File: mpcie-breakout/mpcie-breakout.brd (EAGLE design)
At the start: 50 x 70 mm, 37 parts, among them K1 694108106102, U1 IP4234CZ6, U2 LD1085D2T33R, X1 MPCIE-JAE, X2 MINI-USB-SHIELD-UX60-MB-5ST

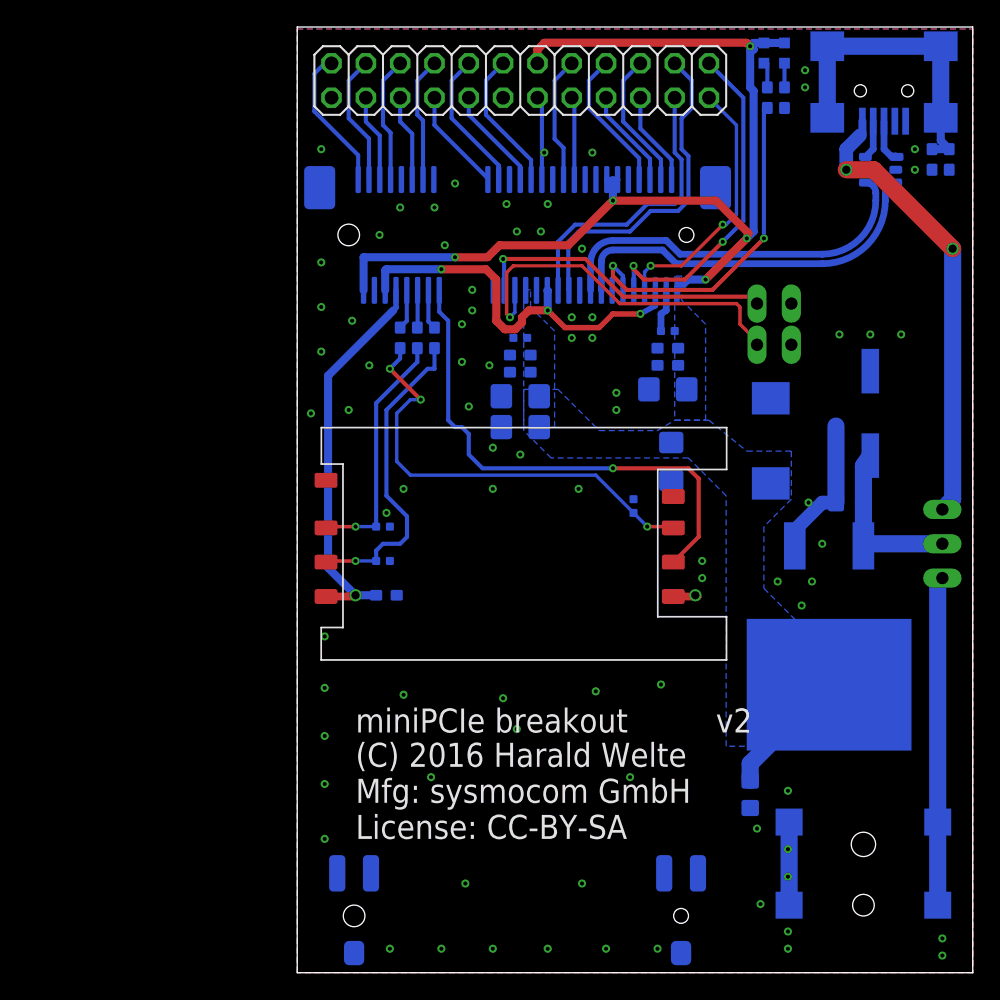
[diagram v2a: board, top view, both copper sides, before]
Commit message: mpcie-breakout: Enlarge to 70x70mm, add SMA, U.FL and Mounting Holes
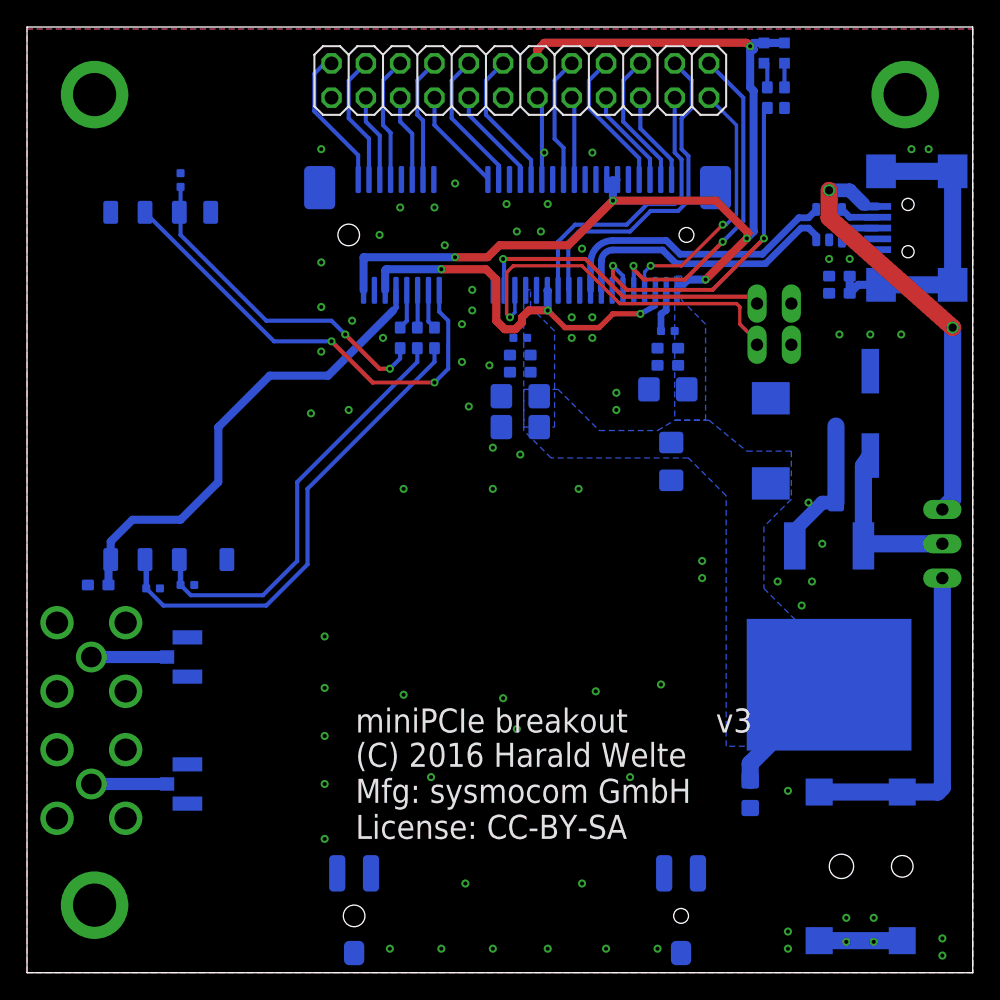
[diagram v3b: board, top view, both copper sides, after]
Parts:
- added X3, X4: (no value), laforge:SMA-F-S-TH
- added X5, X6: (no value), laforge:HRS_UFL
- moved C7 41.3 mm to (-8.64, 58.7)
- moved SIM1 27.5 mm to (-9.91, 43.4), flipped to the bottom, turned to 270 degrees
- moved C8 21.3 mm to (-14.7, 28.7), turned to 180 degrees
- moved C6 17.1 mm to (-10.7, 28.4)
- moved C5 15.1 mm to (-8.13, 28.7)
- moved C9 12.8 mm to (40.1, 50.3), turned to 180 degrees
- moved K1 11.1 mm to (49.8, 7.87), turned to 0 degrees
- moved R4 11.0 mm to (40.1, 51.6), turned to 180 degrees
- moved X2 10.3 mm to (45.2, 55.1), turned to 0 degrees
- moved U1 5.57 mm to (39.4, 55.4), turned to 0 degrees
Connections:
- new net N$13: X3.C, X5.SIG
- new net N$14: X4.C, X6.SIG
- net GND: now also X3.G1, X3.G2, X3.G3, X3.G4, X4.G1, X4.G2, X4.G3, X4.G4, X5.GND@1, X5.GND@2, X6.GND@1, X6.GND@2
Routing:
- net USIM_CLK: track 18.2 -> 31.4 mm, vias 1 -> 0
- net USIM_RESET: track 23.6 -> 35.8 mm, vias 1 -> 0
- net USIM_DATA: track 33.6 -> 25.1 mm, vias 3 -> 2
- net USB_D_P: track 27.5 -> 20.4 mm
- net USB_D_N: track 27.6 -> 21.2 mm
- net USIM_POWER: track 29.2 -> 35.2 mm, vias 1 -> 0
- net N$14: track 0.00 -> 5.61 mm
- net N$13: track 0.00 -> 5.61 mm
- net USIM_VPP: track 38.1 -> 34.2 mm, vias 1 -> 2
- net GND: track 28.3 -> 26.3 mm, vias 82 -> 83
- net USB_VBUS: track 35.4 -> 33.5 mm
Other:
- board size 50 x 70 mm -> 70 x 70 mm

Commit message: mpcie-breakout: Add third U.FL-SMA group
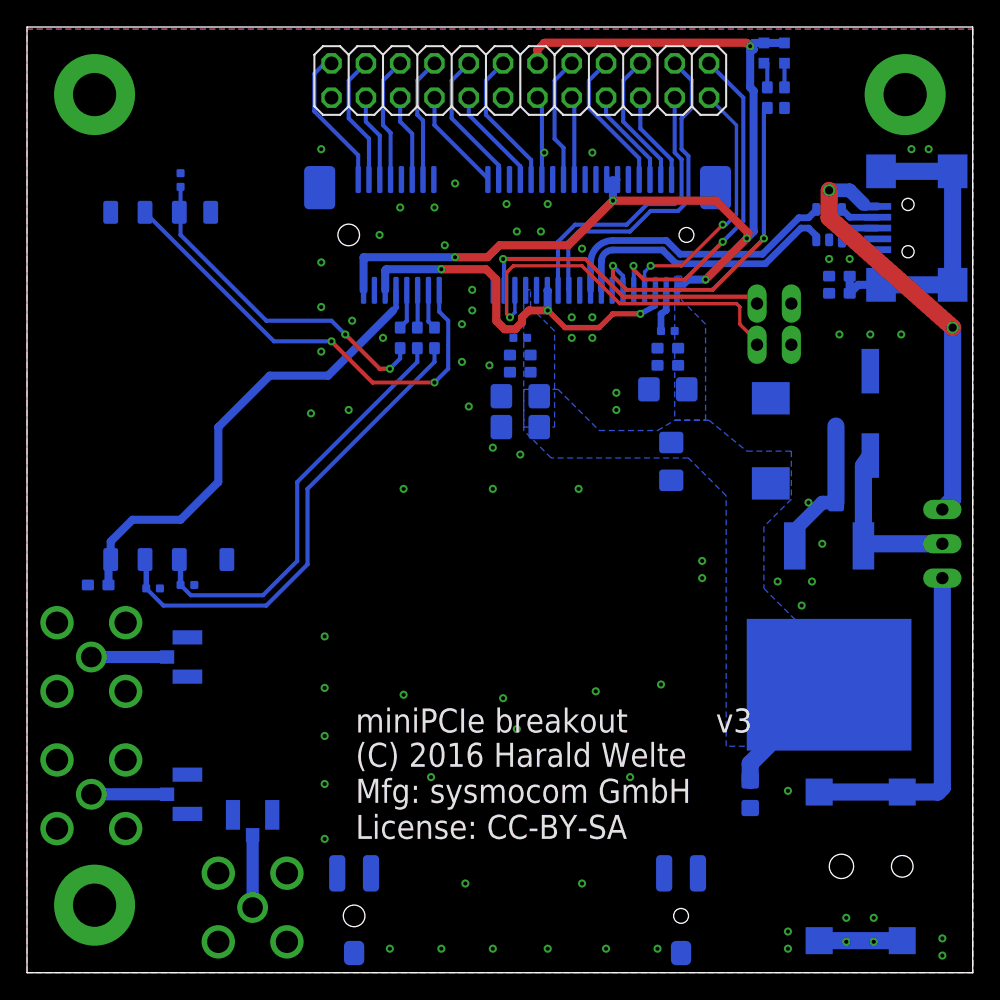
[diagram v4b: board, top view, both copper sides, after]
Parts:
- removed X6: (no value), laforge:HRS_UFL
- added Y3, Y4, Y5: (no value), laforge:HRS_UFL
- X5: device laforge:HRS_UFL -> laforge:SMA-F-S-TH
- moved X5 19.2 mm to (-3.30, 4.83), turned to 0 degrees
- moved X4 0.76 mm to (-15.2, 13.2)
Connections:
- new net N$7: X5.C, Y5.SIG
- net GND: now also X5.G1, X5.G2, X5.G3, X5.G4, Y3.GND@1, Y3.GND@2, Y4.GND@1, Y4.GND@2, Y5.GND@1, Y5.GND@2; no longer X5.GND@1, X5.GND@2, X6.GND@1, X6.GND@2
- net N$13: now also Y3.SIG; no longer X5.SIG
- net N$14: now also Y4.SIG; no longer X6.SIG
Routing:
- net N$7: track 0.00 -> 5.36 mm
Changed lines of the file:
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@@
 </element>
 <element name="X3" library="laforge" package="SMA-F-S-TH" value="" x="-15.24" y="23.368" rot="MR0"/>
-<element name="X4" library="laforge" package="SMA-F-S-TH" value="" x="-15.24" y="13.97" rot="MR180"/>
-<element name="X5" library="laforge" package="HRS_UFL" value="" x="-8.128" y="23.368" rot="MR90">
+<element name="X4" library="laforge" package="SMA-F-S-TH" value="" x="-15.24" y="13.208" rot="MR180"/>
+<element name="Y3" library="laforge" package="HRS_UFL" value="" x="-8.128" y="23.368" rot="MR90">
 <attribute name="OC_DIGIKEY" value="H9161CT-ND" x="-8.128" y="23.368" size="1.778" layer="28" rot="MR90" display="off"/>
 </element>
-<element name="X6" library="laforge" package="HRS_UFL" value="" x="-8.128" y="13.97" rot="MR90">
-<attribute name="OC_DIGIKEY" value="H9161CT-ND" x="-8.128" y="13.97" size="1.778" layer="28" rot="MR90" display="off"/>
+<element name="Y4" library="laforge" package="HRS_UFL" value="" x="-8.128" y="13.208" rot="MR90">
+<attribute name="OC_DIGIKEY" value="H9161CT-ND" x="-8.128" y="13.208" size="1.778" layer="28" rot="MR90" display="off"/>
+</element>
+<element name="X5" library="laforge" package="SMA-F-S-TH" value="" x="-3.302" y="4.826" rot="MR0"/>
+<element name="Y5" library="laforge" package="HRS_UFL" value="" x="-3.302" y="11.684" rot="MR0">
+<attribute name="OC_DIGIKEY" value="H9161CT-ND" x="-3.302" y="11.684" size="1.778" layer="28" rot="MR0" display="off"/>
 </element>
 </elements>
@@
 <contactref element="C11" pad="1"/>
 <contactref element="X3" pad="G1"/>
-<contactref element="X5" pad="GND@1"/>
+<contactref element="Y3" pad="GND@1"/>
 <contactref element="X3" pad="G2"/>
 <contactref element="X3" pad="G3"/>
 <contactref element="X3" pad="G4"/>
-<contactref element="X5" pad="GND@2"/>
+<contactref element="Y3" pad="GND@2"/>
 <contactref element="X4" pad="G1"/>
-<contactref element="X6" pad="GND@1"/>
+<contactref element="Y4" pad="GND@1"/>
 <contactref element="X4" pad="G2"/>
 <contactref element="X4" pad="G3"/>
 <contactref element="X4" pad="G4"/>
-<contactref element="X6" pad="GND@2"/>
-<via x="-15" y="5" extent="1-16" drill="3.2" diameter="5"/>
-<via x="-15" y="65" extent="1-16" drill="3.2" diameter="5"/>
-<via x="45" y="65" extent="1-16" drill="3.2" diameter="5"/>
+<contactref element="Y4" pad="GND@2"/>
+<via x="-15" y="5" extent="1-16" drill="3.2" diameter="6"/>
+<via x="-15" y="65" extent="1-16" drill="3.2" diameter="6"/>
+<via x="45" y="65" extent="1-16" drill="3.2" diameter="6"/>
+<contactref element="X5" pad="G1"/>
+<contactref element="Y5" pad="GND@1"/>
+<contactref element="X5" pad="G2"/>
+<contactref element="X5" pad="G3"/>
+<contactref element="X5" pad="G4"/>
+<contactref element="Y5" pad="GND@2"/>
 </signal>
 <signal name="USIM_POWER" class="3">
@@
 <signal name="N$13" class="2">
 <contactref element="X3" pad="C"/>
-<contactref element="X5" pad="SIG"/>
+<contactref element="Y3" pad="SIG"/>
 <wire x1="-15.24" y1="23.368" x2="-9.6305" y2="23.368" width="0.9" layer="16"/>
 </signal>
 <signal name="N$14" class="2">
 <contactref element="X4" pad="C"/>
-<contactref element="X6" pad="SIG"/>
-<wire x1="-15.24" y1="13.97" x2="-9.6305" y2="13.97" width="0.9" layer="16"/>
+<contactref element="Y4" pad="SIG"/>
+<wire x1="-15.24" y1="13.208" x2="-9.6305" y2="13.208" width="0.9" layer="16"/>
+</signal>
+<signal name="N$7" class="2">
+<contactref element="X5" pad="C"/>
+<contactref element="Y5" pad="SIG"/>
+<wire x1="-3.302" y1="10.1815" x2="-3.302" y2="4.826" width="0.9" layer="16"/>
 </signal>
 </signals>

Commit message: mcie-breakout: Align bLabels, more vias, cosmetics
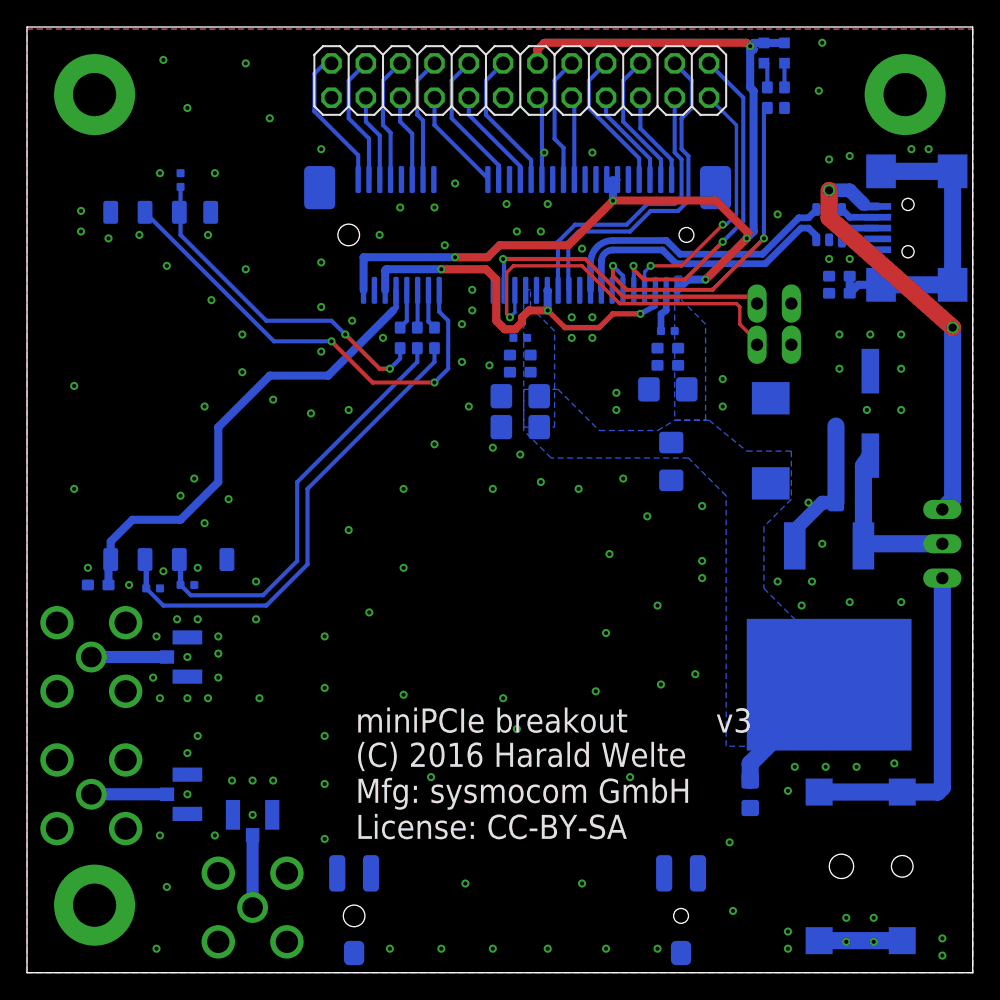
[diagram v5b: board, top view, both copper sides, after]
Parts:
- turned X3 to 180 degrees
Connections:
- net N$4 renamed PERST
- net N$6 renamed W_DISABLE
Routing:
- net GND: vias 83 -> 167
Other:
- board text added: "5V DC"
- board text added: "DC IN"
- board text added: "PERST"
- board text added: "USB"
- board text added: "W_DIS"

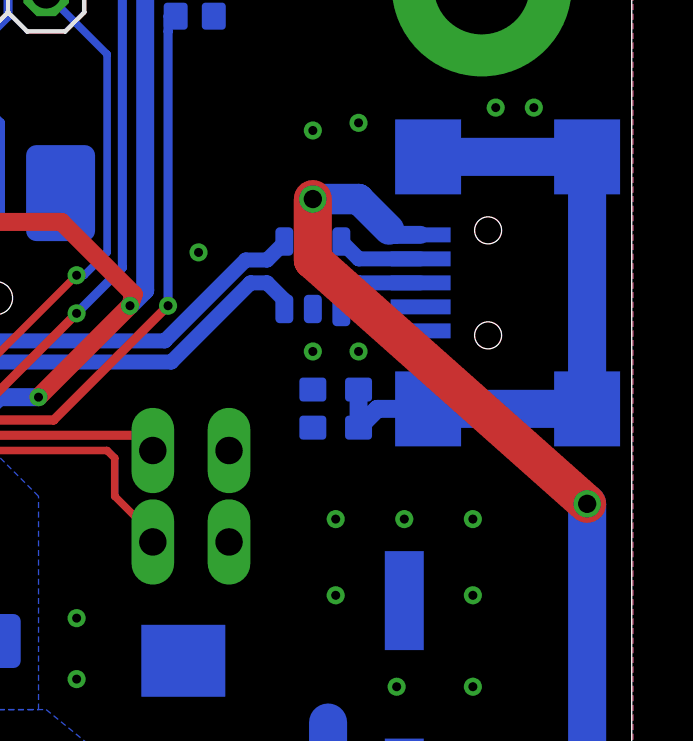
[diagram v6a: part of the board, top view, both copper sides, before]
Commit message: mpcie-breakout: USB_VBUS second parallel via to reduce impedance
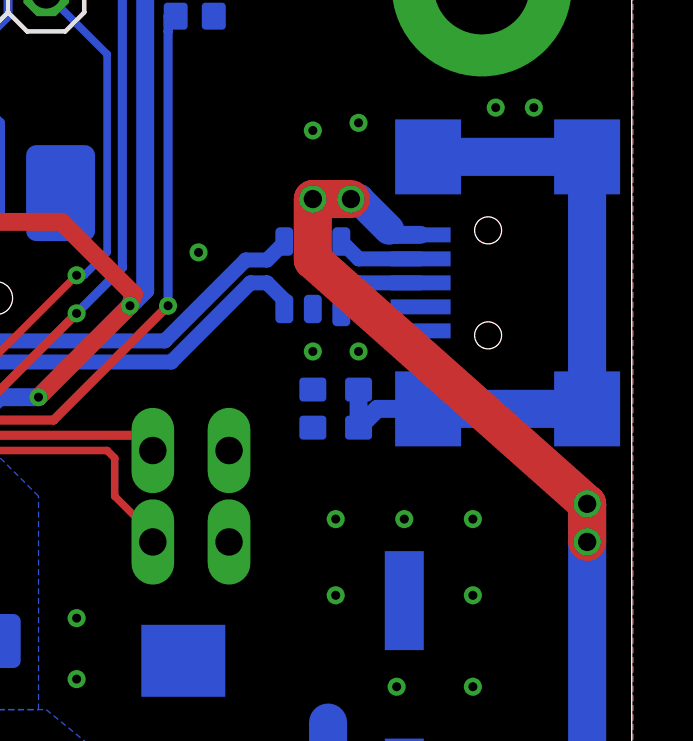
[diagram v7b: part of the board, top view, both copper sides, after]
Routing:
- net USB_VBUS: track 33.5 -> 36.1 mm, vias 2 -> 4
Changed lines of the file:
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@@
 <via x="39.37" y="57.912" extent="1-16" drill="0.6096"/>
 <wire x1="39.37" y1="57.912" x2="40.894" y2="57.912" width="1.016" layer="16"/>
+<via x="48.514" y="46.482" extent="1-16" drill="0.6096"/>
+<wire x1="48.514" y1="47.752" x2="48.514" y2="46.482" width="1.27" layer="1"/>
+<via x="40.64" y="57.912" extent="1-16" drill="0.6096"/>
+<wire x1="39.37" y1="57.912" x2="40.64" y2="57.912" width="1.27" layer="1"/>
 </signal>
 <signal name="WAKE">
